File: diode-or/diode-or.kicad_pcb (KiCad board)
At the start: 2 copper layers, 80.4 x 51.4 mm, 28 parts, among them J1 Binding Post (RED), J2 Binding Post (RED), J3 Binding Post (RED), J4 Binding Post (BLACK), J5 Binding Post (BLACK), Q1 IRFP4710PBF, SW1 SW_SPDT, U1 LM5050-1

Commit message: Use a current source to drive the LED indicator. Update footprints in the diode-or board.
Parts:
- added U2: PSSI2021SAY, Package_TO_SOT_SMD:SOT-353_SC-70-5, B.Cu at (158.8, 111.4)
- HS1: value Heatsink_Pad -> MA-301-27E
- R3: value 14.0K -> 634
- SW1: footprint local:ASE1D-2M-10-Z -> local:ASE1D-6M-10-Z
- moved SW1 5.50 mm to (178.1, 108.0)
- moved R3 1.32 mm to (155.8, 111.4), turned to 270 degrees
- moved D7 0.81 mm to (163.2, 112.0)
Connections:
- D7 pad 1: Net-(D7-Pad1) -> /IOUT
- R3 pad 2: Net-(D7-Pad1) -> /REXT
- SW1 pad 1: Net-(SW1-Pad1) -> /VS_OR
- SW1 pad 3: /VS_OR -> Net-(SW1-Pad3)
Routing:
- net Net-(D7-Pad1): track 2.87 -> 0.00 mm
- net /IOUT: track 0.00 -> 2.27 mm
- net /REXT: track 0.00 -> 2.24 mm
- net /VS: track 30.9 -> 32.8 mm
- net GND: track 4.82 -> 5.97 mm
- net Net-(D7-Pad2): track 5.12 -> 4.58 mm
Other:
- board text added: "+"

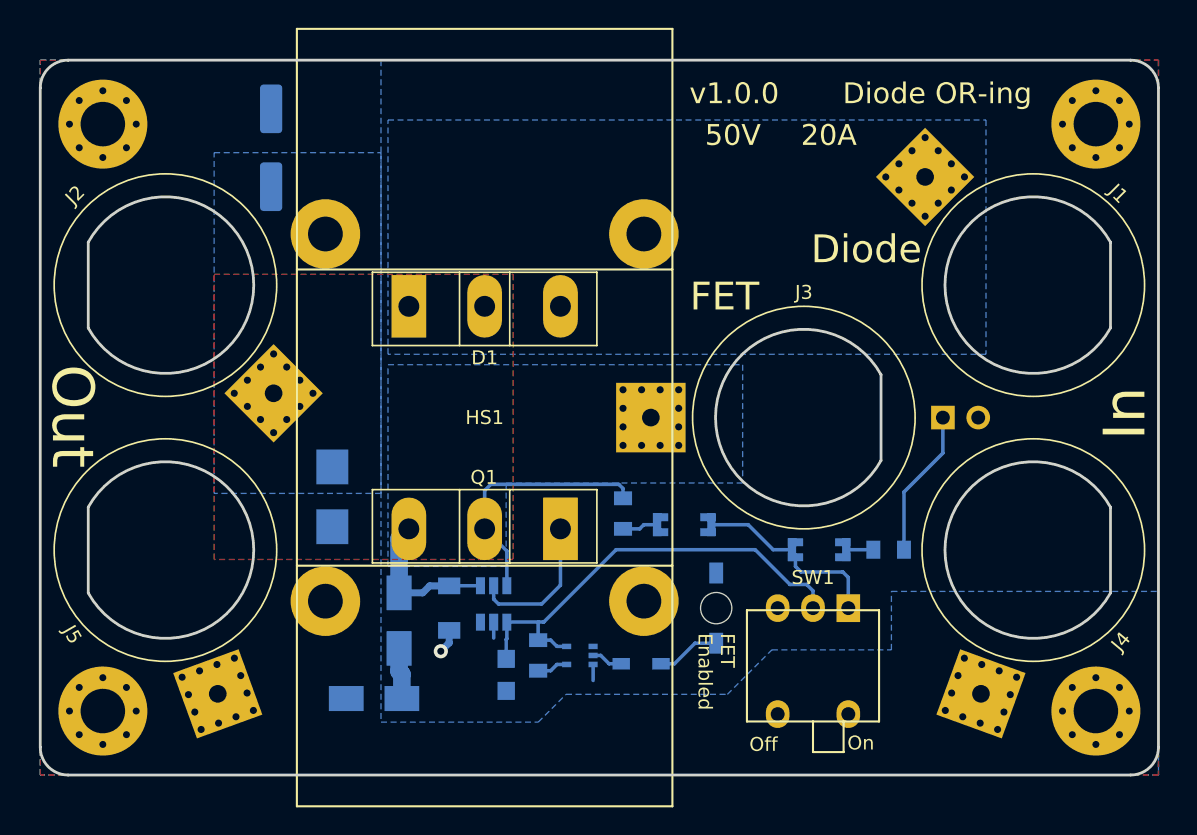
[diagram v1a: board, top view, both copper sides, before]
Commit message: Fix resistor part number. Clean up position of text on the Fab layers.
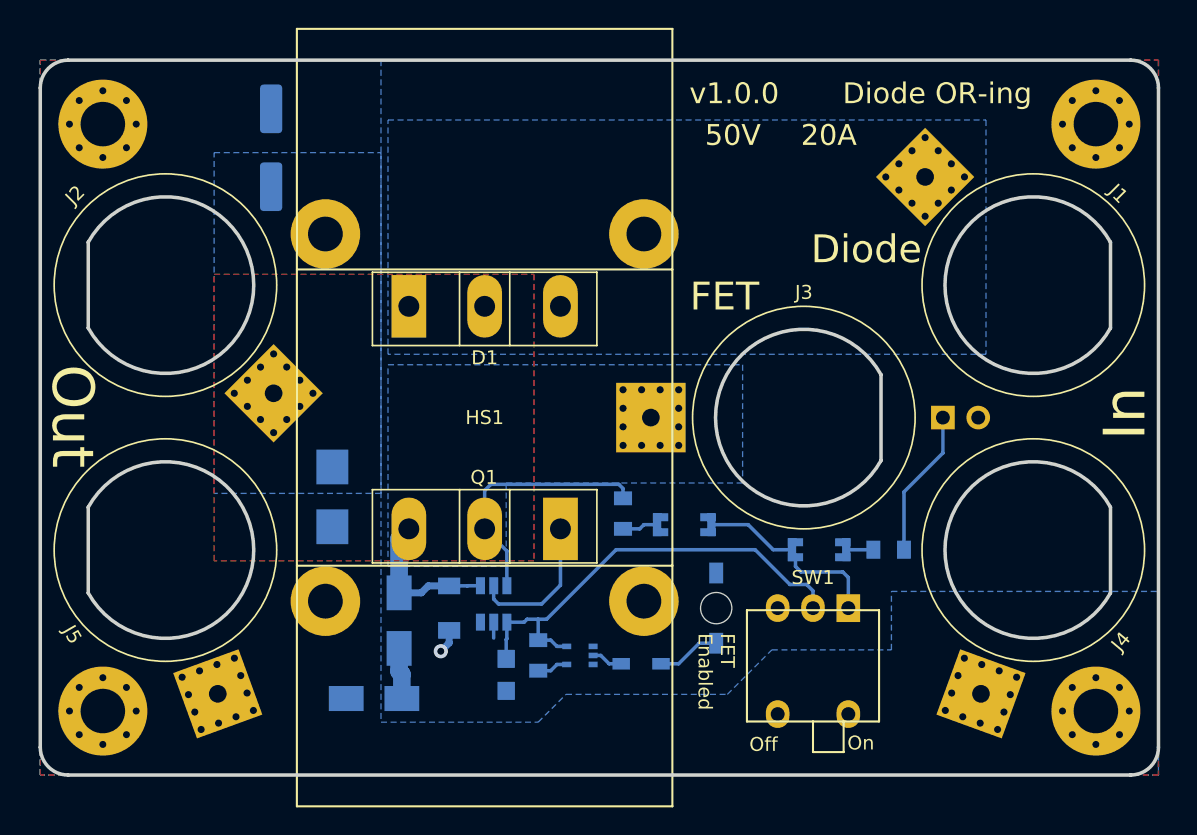
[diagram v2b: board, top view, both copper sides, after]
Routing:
- net GND: track 5.97 -> 4.82 mm

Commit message: Minor change to fill zones. Upload to OSHPark.
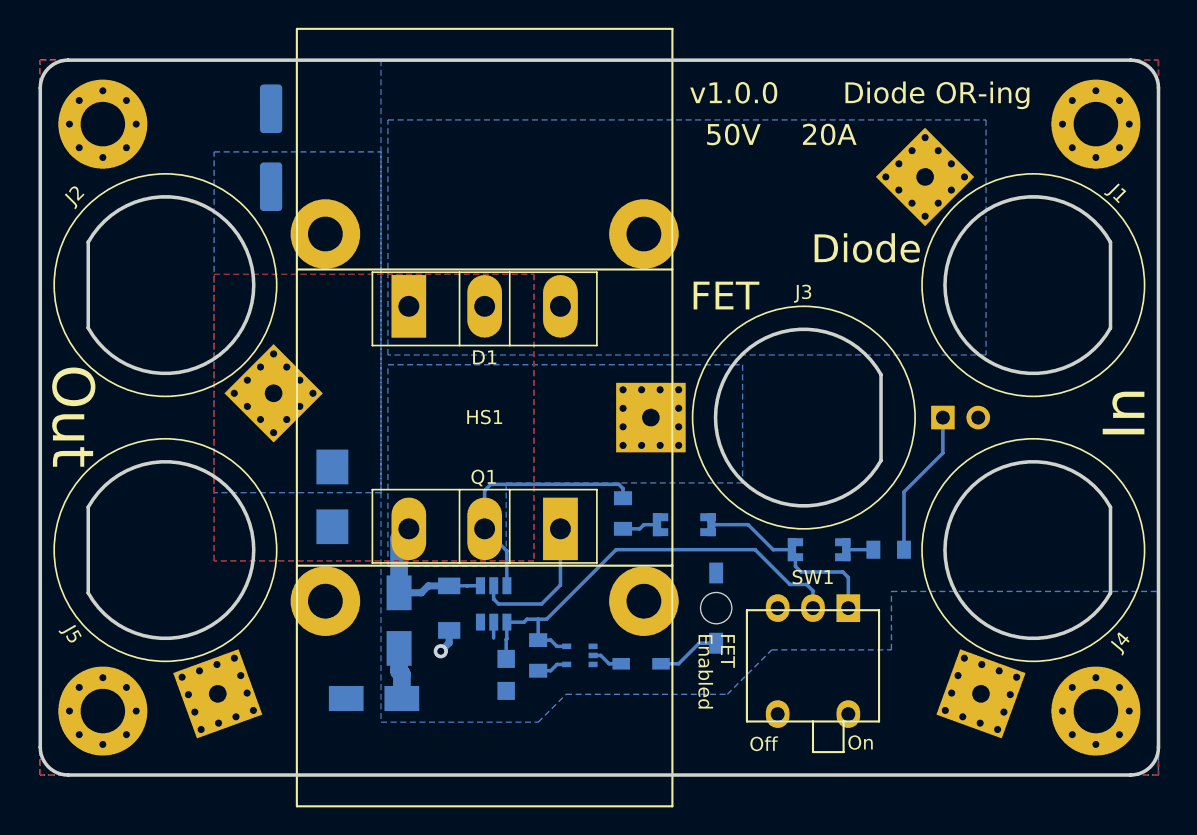
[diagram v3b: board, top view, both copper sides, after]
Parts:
- D7: value MM3Z4V3T1G -> MM3Z3V0T1G
- D8: value LED -> AM2520ZGC09
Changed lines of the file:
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@@
       (effects (font (size 1 1) (thickness 0.15)) (justify mirror))
     )
-    (fp_text value LED (at 0 -2.2 90) (layer B.Fab)
+    (fp_text value AM2520ZGC09 (at 0 -2.2 90) (layer B.Fab)
       (effects (font (size 1 1) (thickness 0.15)) (justify mirror))
     )
@@
       (effects (font (size 1 1) (thickness 0.15)) (justify mirror))
     )
-    (fp_text value MM3Z4V3T1G (at 1.3 -1.5) (layer B.Fab)
+    (fp_text value MM3Z3V0T1G (at 1.3 -1.5) (layer B.Fab)
       (effects (font (size 1 1) (thickness 0.15)) (justify mirror))
     )
@@
     (polygon
       (pts
-        (xy 188 89.75) (xy 145 89.75) (xy 145 72.9) (xy 188 72.9)
+        (xy 188 89.8) (xy 145 89.8) (xy 145 72.9) (xy 188 72.9)
       )
     )
@@
     (polygon
       (pts
-        (xy 144.5 99.75) (xy 132.5 99.75) (xy 132.5 75.25) (xy 144.5 75.25)
+        (xy 144.5 99.7) (xy 132.5 99.7) (xy 132.5 75.2) (xy 144.5 75.2)
       )
     )

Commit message: Change current source resistor value to 4.99k
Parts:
- R3: value 634 -> 4.99K
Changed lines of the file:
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@@
       (effects (font (size 1 1) (thickness 0.15)) (justify mirror))
     )
-    (fp_text value 634 (at -0.1 -1.5 90) (layer B.Fab)
+    (fp_text value 4.99K (at -0.1 -1.5 90) (layer B.Fab)
       (effects (font (size 1 1) (thickness 0.15)) (justify mirror))
     )
